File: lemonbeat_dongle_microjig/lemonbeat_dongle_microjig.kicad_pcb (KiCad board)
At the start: 2 copper layers, 50 x 42 mm, 20 parts, among them J1 Prog, J2 Main, J3 Si4467

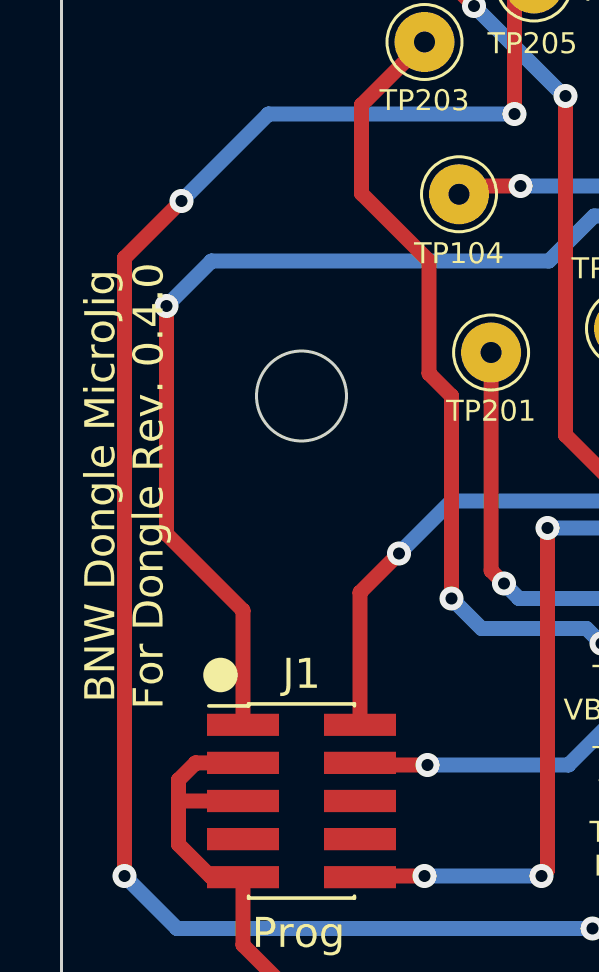
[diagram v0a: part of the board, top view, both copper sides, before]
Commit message: dongle & micro jig: update revision to 0.4.1
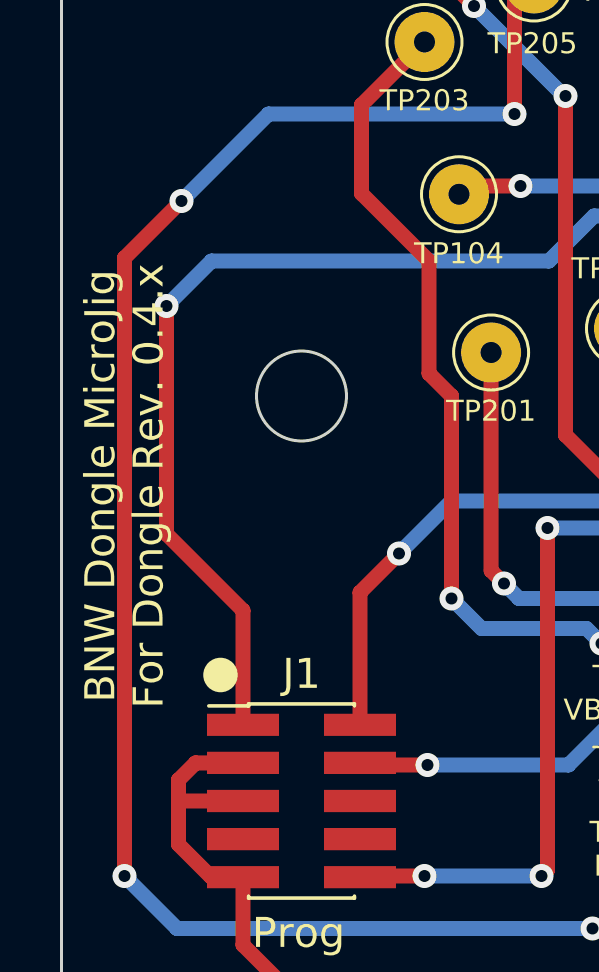
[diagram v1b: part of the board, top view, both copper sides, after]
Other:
- board text added: "BNW Dongle MicroJig For Dongle Rev. 0.4.x"
- board text removed: "BNW Dongle MicroJig For Dongle Rev. 0.4.0"
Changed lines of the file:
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@@
 				(font
 					(size 1.27 1.27)
+					(thickness 0.15)
 				)
 			)
@@
 				(font
 					(size 1.27 1.27)
+					(thickness 0.15)
 				)
 			)
@@
 				(font
 					(size 1.27 1.27)
+					(thickness 0.15)
 				)
 			)
@@
 				(font
 					(size 1.27 1.27)
+					(thickness 0.15)
 				)
 			)
@@
 				(font
 					(size 1.27 1.27)
+					(thickness 0.15)
 				)
 			)
@@
 				(font
 					(size 1.27 1.27)
+					(thickness 0.15)
 				)
 			)
@@
 				(font
 					(size 1.27 1.27)
+					(thickness 0.15)
 				)
 			)
@@
 				(font
 					(size 1.27 1.27)
+					(thickness 0.15)
 				)
 			)
@@
 				(font
 					(size 1.27 1.27)
+					(thickness 0.15)
 				)
 			)
@@
 				(font
 					(size 1.27 1.27)
+					(thickness 0.15)
 				)
 			)
@@
 				(font
 					(size 1.27 1.27)
+					(thickness 0.15)
 				)
 			)
@@
 				(font
 					(size 1.27 1.27)
+					(thickness 0.15)
 				)
 			)
@@
 				(font
 					(size 1.27 1.27)
+					(thickness 0.15)
 				)
 			)
@@
 				(font
 					(size 1.27 1.27)
+					(thickness 0.15)
 				)
 			)
@@
 				(font
 					(size 1.27 1.27)
+					(thickness 0.15)
 				)
 			)
@@
 				(font
 					(size 1.27 1.27)
+					(thickness 0.15)
 				)
 			)
@@
 				(font
 					(size 1.27 1.27)
+					(thickness 0.15)
 				)
 			)
@@
 				(font
 					(size 1.27 1.27)
+					(thickness 0.15)
 				)
 			)
@@
 				(font
 					(size 1.27 1.27)
+					(thickness 0.15)
 				)
 			)
@@
 				(font
 					(size 1.27 1.27)
+					(thickness 0.15)
 				)
 			)
@@
 				(font
 					(size 1.27 1.27)
+					(thickness 0.15)
 				)
 			)
@@
 				(font
 					(size 1.27 1.27)
+					(thickness 0.15)
 				)
 			)
@@
 				(font
 					(size 1.27 1.27)
+					(thickness 0.15)
 				)
 			)
@@
 				(font
 					(size 1.27 1.27)
+					(thickness 0.15)
 				)
 			)
@@
 				(font
 					(size 1.27 1.27)
+					(thickness 0.15)
 				)
 			)
@@
 				(font
 					(size 1.27 1.27)
+					(thickness 0.15)
 				)
 			)
@@
 				(font
 					(size 1.27 1.27)
+					(thickness 0.15)
 				)
 			)
@@
 				(font
 					(size 1.27 1.27)
+					(thickness 0.15)
 				)
 			)
@@
 				(font
 					(size 1.27 1.27)
+					(thickness 0.15)
 				)
 			)
@@
 				(font
 					(size 1.27 1.27)
+					(thickness 0.15)
 				)
 			)
@@
 				(font
 					(size 1.27 1.27)
+					(thickness 0.15)
 				)
 			)
@@
 				(font
 					(size 1.27 1.27)
+					(thickness 0.15)
 				)
 			)
@@
 				(font
 					(size 1.27 1.27)
+					(thickness 0.15)
 				)
 			)
@@
 				(font
 					(size 1.27 1.27)
+					(thickness 0.15)
 				)
 			)
@@
 				(font
 					(size 1.27 1.27)
+					(thickness 0.15)
 				)
 			)
@@
 				(font
 					(size 1.27 1.27)
+					(thickness 0.15)
 				)
 			)
@@
 				(font
 					(size 1.27 1.27)
+					(thickness 0.15)
 				)
 			)
@@
 				(font
 					(size 1.27 1.27)
+					(thickness 0.15)
 				)
 			)
@@
 				(font
 					(size 1.27 1.27)
+					(thickness 0.15)
 				)
 			)
@@
 				(font
 					(size 1.27 1.27)
+					(thickness 0.15)
 				)
 			)
@@
 				(font
 					(size 1.27 1.27)
+					(thickness 0.15)
 				)
 			)
@@
 				(font
 					(size 1.27 1.27)
+					(thickness 0.15)
 				)
 			)
@@
 				(font
 					(size 1.27 1.27)
+					(thickness 0.15)
 				)
 			)
@@
 				(font
 					(size 1.27 1.27)
+					(thickness 0.15)
 				)
 			)
@@
 				(font
 					(size 1.27 1.27)
+					(thickness 0.15)
 				)
 			)
@@
 				(font
 					(size 1.27 1.27)
+					(thickness 0.15)
 				)
 			)
@@
 				(font
 					(size 1.27 1.27)
+					(thickness 0.15)
 				)
 			)
@@
 				(font
 					(size 1.27 1.27)
+					(thickness 0.15)
 				)
 			)
@@
 				(font
 					(size 1.27 1.27)
+					(thickness 0.15)
 				)
 			)
@@
 				(font
 					(size 1.27 1.27)
+					(thickness 0.15)
 				)
 			)
@@
 				(font
 					(size 1.27 1.27)
+					(thickness 0.15)
 				)
 			)
@@
 				(font
 					(size 1.27 1.27)
+					(thickness 0.15)
 				)
 			)
@@
 				(font
 					(size 1.27 1.27)
+					(thickness 0.15)
 				)
 			)
@@
 				(font
 					(size 1.27 1.27)
+					(thickness 0.15)
 				)
 			)
@@
 				(font
 					(size 1.27 1.27)
+					(thickness 0.15)
 				)
 			)
@@
 				(font
 					(size 1.27 1.27)
+					(thickness 0.15)
 				)
 			)
@@
 				(font
 					(size 1.27 1.27)
+					(thickness 0.15)
 				)
 			)
@@
 				(font
 					(size 1.27 1.27)
+					(thickness 0.15)
 				)
 			)
@@
 				(font
 					(size 1.27 1.27)
+					(thickness 0.15)
 				)
 			)
@@
 				(font
 					(size 1.27 1.27)
+					(thickness 0.15)
 				)
 			)
@@
 		(layer "Edge.Cuts")
 	)
-	(gr_text "BNW Dongle MicroJig\nFor Dongle Rev. 0.4.0"
+	(gr_text "BNW Dongle MicroJig\nFor Dongle Rev. 0.4.x"
 		(at 112.6 114.5 90)
 		(layer "F.SilkS")

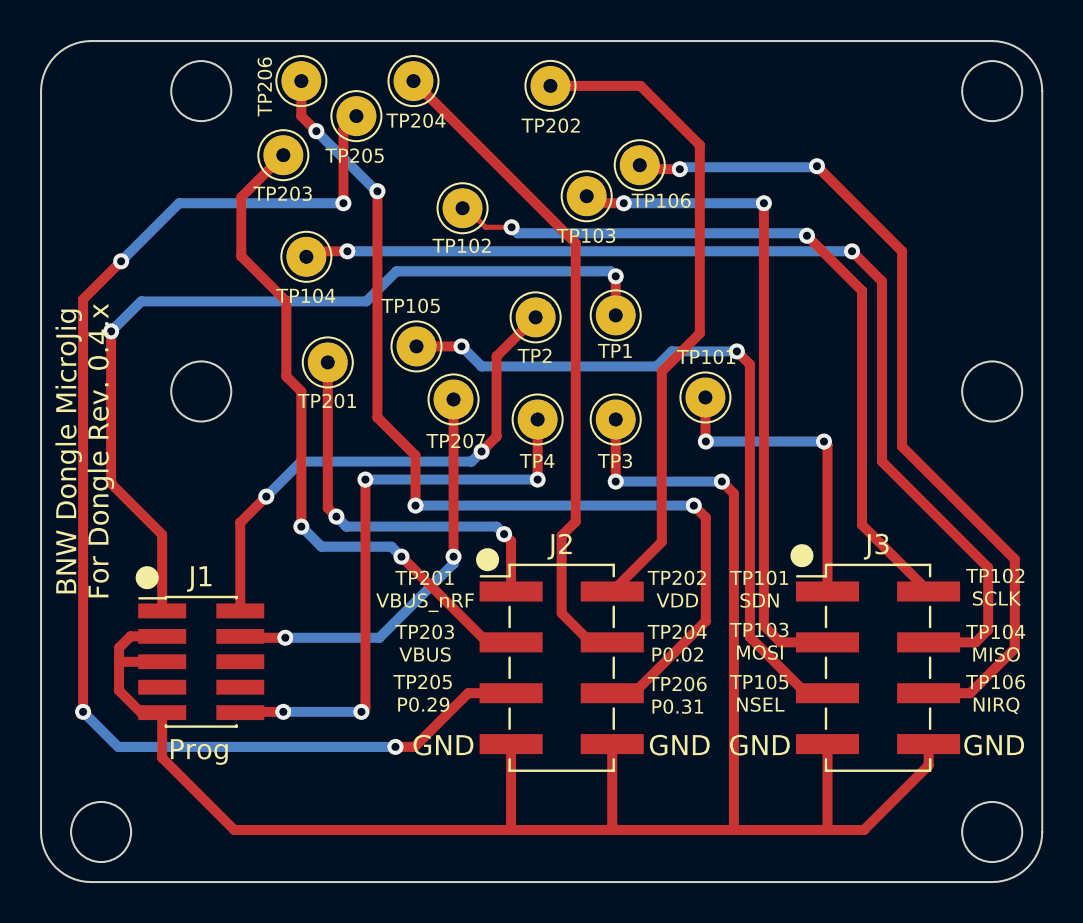
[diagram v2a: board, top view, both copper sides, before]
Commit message: dongle: microjig: PCB: fix DRC errors for KiCad 9
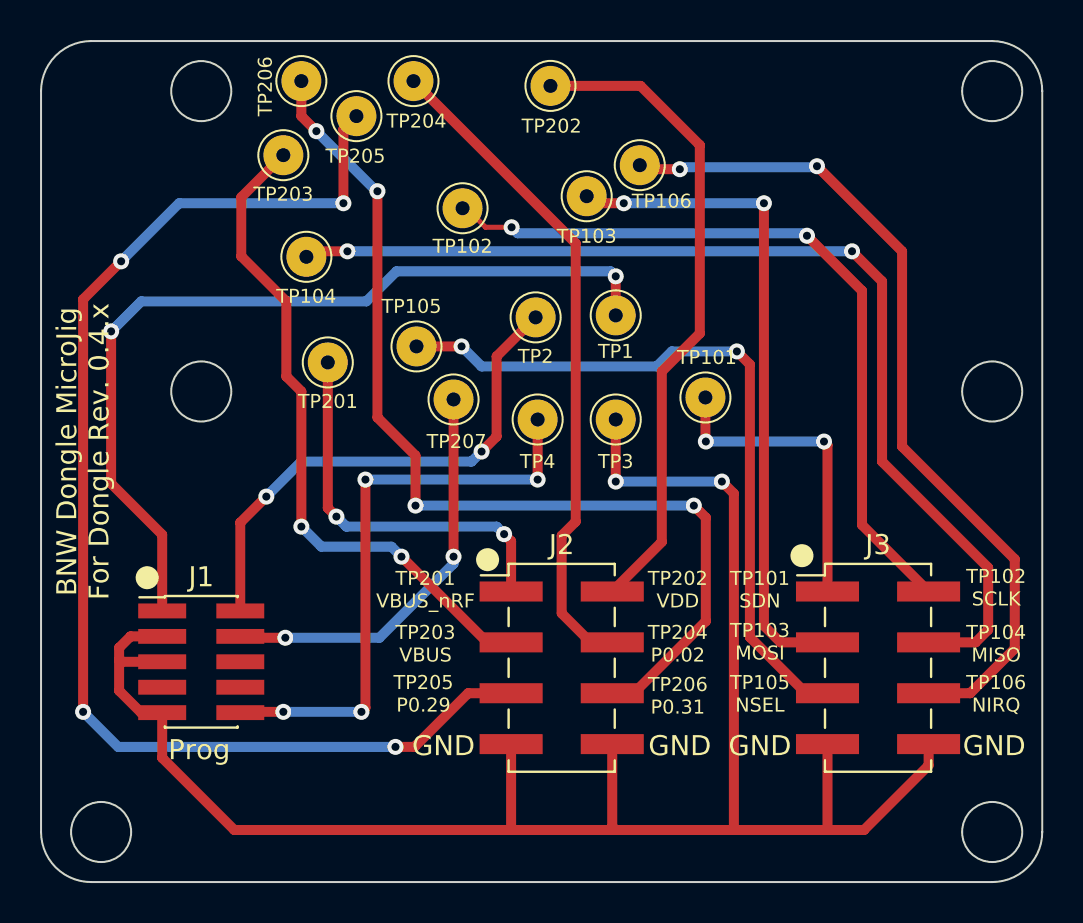
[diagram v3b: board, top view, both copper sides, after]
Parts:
- TP101, TP102, TP103, TP104, TP105, TP106: value TestPoint_Small -> TestPoint
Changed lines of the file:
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@@
 		(attr smd)
 		(fp_line
-			(start -4.04 -4.57)
-			(end -2.6 -4.57)
+			(start -4.04 -4.62)
+			(end -2.65 -4.62)
 			(stroke
 				(width 0.12)
@@
 		)
 		(fp_line
-			(start -2.6 -5.14)
-			(end -2.6 -4.57)
+			(start -2.65 -5.19)
+			(end -2.65 -4.62)
 			(stroke
 				(width 0.12)
@@
 		)
 		(fp_line
-			(start -2.6 -5.14)
-			(end 2.6 -5.14)
+			(start -2.65 -5.19)
+			(end 2.65 -5.19)
 			(stroke
 				(width 0.12)
@@
 		)
 		(fp_line
-			(start -2.6 -3.05)
-			(end -2.6 -2.03)
+			(start -2.65 -3)
+			(end -2.65 -2.08)
 			(stroke
 				(width 0.12)
@@
 		)
 		(fp_line
-			(start -2.6 -0.51)
-			(end -2.6 0.51)
+			(start -2.65 -0.46)
+			(end -2.65 0.46)
 			(stroke
 				(width 0.12)
@@
 		)
 		(fp_line
-			(start -2.6 2.03)
-			(end -2.6 3.05)
+			(start -2.65 2.08)
+			(end -2.65 3)
 			(stroke
 				(width 0.12)
@@
 		)
 		(fp_line
-			(start -2.6 4.57)
-			(end -2.6 5.14)
+			(start -2.65 4.62)
+			(end -2.65 5.19)
 			(stroke
 				(width 0.12)
@@
 		)
 		(fp_line
-			(start -2.6 5.14)
-			(end 2.6 5.14)
+			(start -2.65 5.19)
+			(end 2.65 5.19)
 			(stroke
 				(width 0.12)
@@
 		)
 		(fp_line
-			(start 2.6 -5.14)
-			(end 2.6 -4.57)
+			(start 2.65 -5.19)
+			(end 2.65 -4.62)
 			(stroke
 				(width 0.12)
@@
 		)
 		(fp_line
-			(start 2.6 -3.05)
-			(end 2.6 -2.03)
+			(start 2.65 -3)
+			(end 2.65 -2.08)
 			(stroke
 				(width 0.12)
@@
 		)
 		(fp_line
-			(start 2.6 -0.51)
-			(end 2.6 0.51)
+			(start 2.65 -0.46)
+			(end 2.65 0.46)
 			(stroke
 				(width 0.12)
@@
 		)
 		(fp_line
-			(start 2.6 2.03)
-			(end 2.6 3.05)
+			(start 2.65 2.08)
+			(end 2.65 3)
 			(stroke
 				(width 0.12)
@@
 		)
 		(fp_line
-			(start 2.6 4.57)
-			(end 2.6 5.14)
+			(start 2.65 4.62)
+			(end 2.65 5.19)
 			(stroke
 				(width 0.12)
@@
 		)
 		(fp_line
-			(start -5.9 -5.6)
-			(end -5.9 5.6)
+			(start -5.87 -5.58)
+			(end -5.87 5.58)
 			(stroke
 				(width 0.05)
@@
 		)
 		(fp_line
-			(start -5.9 5.6)
-			(end 5.9 5.6)
+			(start -5.87 5.58)
+			(end 5.88 5.58)
 			(stroke
 				(width 0.05)
@@
 		)
 		(fp_line
-			(start 5.9 -5.6)
-			(end -5.9 -5.6)
+			(start 5.88 -5.58)
+			(end -5.87 -5.58)
 			(stroke
 				(width 0.05)
@@
 		)
 		(fp_line
-			(start 5.9 5.6)
-			(end 5.9 -5.6)
+			(start 5.88 5.58)
+			(end 5.88 -5.58)
 			(stroke
 				(width 0.05)
@@
 		(attr smd)
 		(fp_line
-			(start -4.04 -4.57)
-			(end -2.6 -4.57)
+			(start -4.04 -4.62)
+			(end -2.65 -4.62)
 			(stroke
 				(width 0.12)
@@
 		)
 		(fp_line
-			(start -2.6 -5.14)
-			(end -2.6 -4.57)
+			(start -2.65 -5.19)
+			(end -2.65 -4.62)
 			(stroke
 				(width 0.12)
@@
 		)
 		(fp_line
-			(start -2.6 -5.14)
-			(end 2.6 -5.14)
+			(start -2.65 -5.19)
+			(end 2.65 -5.19)
 			(stroke
 				(width 0.12)
@@
 		)
 		(fp_line
-			(start -2.6 -3.05)
-			(end -2.6 -2.03)
+			(start -2.65 -3)
+			(end -2.65 -2.08)
 			(stroke
 				(width 0.12)
@@
 		)
 		(fp_line
-			(start -2.6 -0.51)
-			(end -2.6 0.51)
+			(start -2.65 -0.46)
+			(end -2.65 0.46)
 			(stroke
 				(width 0.12)
@@
 		)
 		(fp_line
-			(start -2.6 2.03)
-			(end -2.6 3.05)
+			(start -2.65 2.08)
+			(end -2.65 3)
 			(stroke
 				(width 0.12)
@@
 		)
 		(fp_line
-			(start -2.6 4.57)
-			(end -2.6 5.14)
+			(start -2.65 4.62)
+			(end -2.65 5.19)
 			(stroke
 				(width 0.12)
@@
 		)
 		(fp_line
-			(start -2.6 5.14)
-			(end 2.6 5.14)
+			(start -2.65 5.19)
+			(end 2.65 5.19)
 			(stroke
 				(width 0.12)
@@
 		)
 		(fp_line
-			(start 2.6 -5.14)
-			(end 2.6 -4.57)
+			(start 2.65 -5.19)
+			(end 2.65 -4.62)
 			(stroke
 				(width 0.12)
@@
 		)
 		(fp_line
-			(start 2.6 -3.05)
-			(end 2.6 -2.03)
+			(start 2.65 -3)
+			(end 2.65 -2.08)
 			(stroke
 				(width 0.12)
@@
 		)
 		(fp_line
-			(start 2.6 -0.51)
-			(end 2.6 0.51)
+			(start 2.65 -0.46)
+			(end 2.65 0.46)
 			(stroke
 				(width 0.12)
@@
 		)
 		(fp_line
-			(start 2.6 2.03)
-			(end 2.6 3.05)
+			(start 2.65 2.08)
+			(end 2.65 3)
 			(stroke
 				(width 0.12)
@@
 		)
 		(fp_line
-			(start 2.6 4.57)
-			(end 2.6 5.14)
+			(start 2.65 4.62)
+			(end 2.65 5.19)
 			(stroke
 				(width 0.12)
@@
 		)
 		(fp_line
-			(start -5.9 -5.6)
-			(end -5.9 5.6)
+			(start -5.87 -5.58)
+			(end -5.87 5.58)
 			(stroke
 				(width 0.05)
@@
 		)
 		(fp_line
-			(start -5.9 5.6)
-			(end 5.9 5.6)
+			(start -5.87 5.58)
+			(end 5.88 5.58)
 			(stroke
 				(width 0.05)
@@
 		)
 		(fp_line
-			(start 5.9 -5.6)
-			(end -5.9 -5.6)
+			(start 5.88 -5.58)
+			(end -5.87 -5.58)
 			(stroke
 				(width 0.05)
@@
 		)
 		(fp_line
-			(start 5.9 5.6)
-			(end 5.9 -5.6)
+			(start 5.88 5.58)
+			(end 5.88 -5.58)
 			(stroke
 				(width 0.05)
@@
 			)
 		)
-		(property "Value" "TestPoint_Small"
+		(property "Value" "TestPoint"
 			(at 0 2.05 0)
 			(layer "F.Fab")
@@
 			)
 		)
-		(property "Value" "TestPoint_Small"
+		(property "Value" "TestPoint"
 			(at 0 2.05 0)
 			(layer "F.Fab")
@@
 		(attr smd)
 		(fp_line
-			(start -3.09 -3.17)
-			(end -1.765 -3.17)
+			(start -3.09 -3.22)
+			(end -1.815 -3.22)
 			(stroke
 				(width 0.12)
@@
 		)
 		(fp_line
-			(start -1.765 -3.235)
-			(end -1.765 -3.17)
+			(start -1.815 -3.285)
+			(end -1.815 -3.22)
 			(stroke
 				(width 0.12)
@@
 		)
 		(fp_line
-			(start -1.765 -3.235)
-			(end 1.765 -3.235)
+			(start -1.815 -3.285)
+			(end 1.815 -3.285)
 			(stroke
 				(width 0.12)
@@
 		)
 		(fp_line
-			(start -1.765 3.17)
-			(end -1.765 3.235)
+			(start -1.815 3.22)
+			(end -1.815 3.285)
 			(stroke
 				(width 0.12)
@@
 		)
 		(fp_line
-			(start -1.765 3.235)
-			(end 1.765 3.235)
+			(start -1.815 3.285)
+			(end 1.815 3.285)
 			(stroke
 				(width 0.12)
@@
 		)
 		(fp_line
-			(start 1.765 -3.235)
-			(end 1.765 -3.17)
+			(start 1.815 -3.285)
+			(end 1.815 -3.22)
 			(stroke
 				(width 0.12)
@@
 		)
 		(fp_line
-			(start 1.765 3.17)
-			(end 1.765 3.235)
+			(start 1.815 3.22)
+			(end 1.815 3.285)
 			(stroke
 				(width 0.12)
@@
 		)
 		(fp_line
-			(start -4.3 -3.7)
-			(end -4.3 3.7)
+			(start -4.29 -3.68)
+			(end -4.29 3.68)
 			(stroke
 				(width 0.05)
@@
 		)
 		(fp_line
-			(start -4.3 3.7)
-			(end 4.3 3.7)
+			(start -4.29 3.68)
+			(end 4.29 3.68)
 			(stroke
 				(width 0.05)
@@
 		)
 		(fp_line
-			(start 4.3 -3.7)
-			(end -4.3 -3.7)
+			(start 4.29 -3.68)
+			(end -4.29 -3.68)
 			(stroke
 				(width 0.05)
@@
 		)
 		(fp_line
-			(start 4.3 3.7)
-			(end 4.3 -3.7)
+			(start 4.29 3.68)
+			(end 4.29 -3.68)
 			(stroke
 				(width 0.05)
@@
 			)
 		)
-		(property "Value" "TestPoint_Small"
+		(property "Value" "TestPoint"
 			(at 0 2.05 0)
 			(layer "F.Fab")
@@
 			)
 		)
-		(property "Value" "TestPoint_Small"
+		(property "Value" "TestPoint"
 			(at 0 2.05 0)
 			(layer "F.Fab")
@@
 			)
 		)
-		(property "Value" "TestPoint_Small"
+		(property "Value" "TestPoint"
 			(at 0 2.05 0)
 			(layer "F.Fab")
@@
 			)
 		)
-		(property "Value" "TestPoint_Small"
+		(property "Value" "TestPoint"
 			(at 0 2.05 0)
 			(layer "F.Fab")
